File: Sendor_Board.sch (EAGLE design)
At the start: 36 parts, among them Q1 8.000Mhz, U1 PIC32MX795F512H-80I/PT, U2 SHT25, U3 MPL115A2, U4 MRF24J40MA, X1 MINI-USB-SHIELD-UX60A-MB-5ST

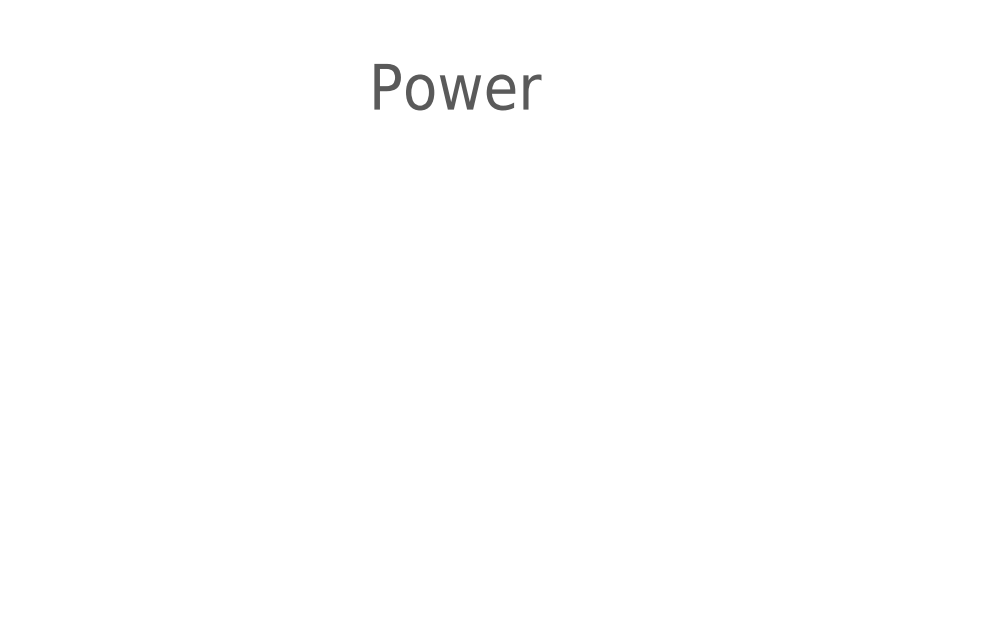
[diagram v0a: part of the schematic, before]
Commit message: Add 3,3V decoupling capacitor
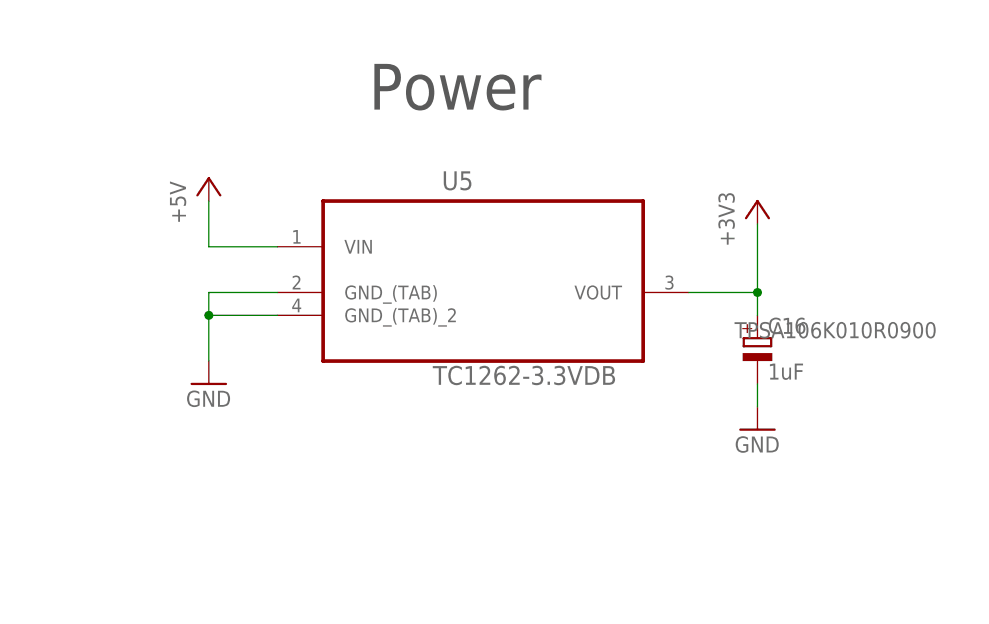
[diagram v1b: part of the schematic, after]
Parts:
- added C16: 1uF, resistor:CPOL-EUA/3216-18W
- added U5: TC1262-3.3VDB, pfo:TC1262-3.3VDB
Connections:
- net +3V3: now also C16.+, U5.VOUT
- net +5V: now also U5.VIN
- net GND: now also C16.-, U5.GND_(TAB), U5.GND_(TAB)_2
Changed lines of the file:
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@@
 <part name="X2" library="con-phoenix-254" deviceset="MPT2" device=""/>
 <part name="FRAME1" library="frames" deviceset="A3L-LOC" device=""/>
+<part name="U5" library="pfo" deviceset="TC1262-3.3VDB" device=""/>
+<part name="P+3" library="supply1" deviceset="+5V" device=""/>
+<part name="GND15" library="supply1" deviceset="GND" device=""/>
+<part name="+3V6" library="supply1" deviceset="+3V3" device=""/>
+<part name="C16" library="resistor" deviceset="CPOL-EU" device="A/3216-18W" value="1uF">
+<attribute name="TYPE" value="TPSA106K010R0900"/>
+</part>
+<part name="GND16" library="supply1" deviceset="GND" device=""/>
 </parts>
 <sheets>
@@
 <instance part="X2" gate="-2" x="144.78" y="-88.9"/>
 <instance part="FRAME1" gate="G$1" x="-111.76" y="-142.24"/>
+<instance part="U5" gate="A" x="208.28" y="-33.02"/>
+<instance part="P+3" gate="1" x="177.8" y="-25.4"/>
+<instance part="GND15" gate="1" x="177.8" y="-48.26"/>
+<instance part="+3V6" gate="G$1" x="238.76" y="-27.94"/>
+<instance part="C16" gate="G$1" x="238.76" y="-43.18">
+<attribute name="TYPE" x="236.22" y="-43.18" size="1.778" layer="96"/>
+</instance>
+<instance part="GND16" gate="1" x="238.76" y="-53.34"/>
 </instances>
 <busses>
@@
 <wire x1="68.58" y1="-124.46" x2="68.58" y2="-127" width="0.1524" layer="91"/>
 </segment>
+<segment>
+<pinref part="U5" gate="A" pin="GND_(TAB)"/>
+<pinref part="GND15" gate="1" pin="GND"/>
+<wire x1="185.42" y1="-38.1" x2="177.8" y2="-38.1" width="0.1524" layer="91"/>
+<wire x1="177.8" y1="-38.1" x2="177.8" y2="-40.64" width="0.1524" layer="91"/>
+<pinref part="U5" gate="A" pin="GND_(TAB)_2"/>
+<wire x1="177.8" y1="-40.64" x2="177.8" y2="-45.72" width="0.1524" layer="91"/>
+<wire x1="185.42" y1="-40.64" x2="177.8" y2="-40.64" width="0.1524" layer="91"/>
+<junction x="177.8" y="-40.64"/>
+</segment>
+<segment>
+<pinref part="C16" gate="G$1" pin="-"/>
+<pinref part="GND16" gate="1" pin="GND"/>
+<wire x1="238.76" y1="-48.26" x2="238.76" y2="-50.8" width="0.1524" layer="91"/>
+</segment>
 </net>
 <net name="+3V3" class="0">
@@
 <junction x="96.52" y="-15.24"/>
 </segment>
+<segment>
+<pinref part="+3V6" gate="G$1" pin="+3V3"/>
+<wire x1="238.76" y1="-30.48" x2="238.76" y2="-38.1" width="0.1524" layer="91"/>
+<pinref part="U5" gate="A" pin="VOUT"/>
+<wire x1="238.76" y1="-38.1" x2="231.14" y2="-38.1" width="0.1524" layer="91"/>
+<pinref part="C16" gate="G$1" pin="+"/>
+<wire x1="238.76" y1="-40.64" x2="238.76" y2="-38.1" width="0.1524" layer="91"/>
+<junction x="238.76" y="-38.1"/>
+</segment>
 </net>
 <net name="N$1" class="0">
@@
 <wire x1="-93.98" y1="-5.08" x2="-83.82" y2="-5.08" width="0.1524" layer="91"/>
 </segment>
-</net>
+<segment>
+<pinref part="U5" gate="A" pin="VIN"/>
+<pinref part="P+3" gate="1" pin="+5V"/>
+<wire x1="185.42" y1="-33.02" x2="177.8" y2="-33.02" width="0.1524" layer="91"/>
+<wire x1="177.8" y1="-33.02" x2="177.8" y2="-27.94" width="0.1524" layer="91"/>
+</segment>
+</net>

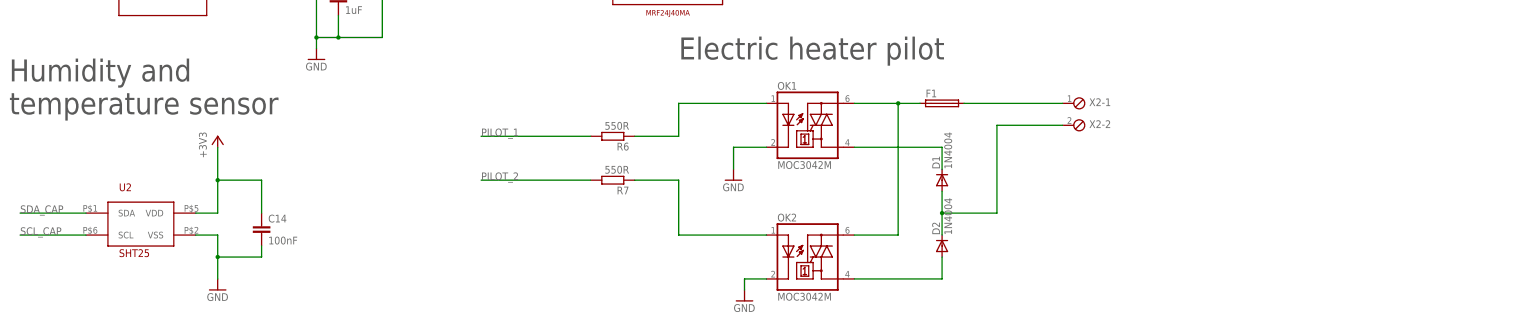
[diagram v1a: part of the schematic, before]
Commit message: Insert Power convertor
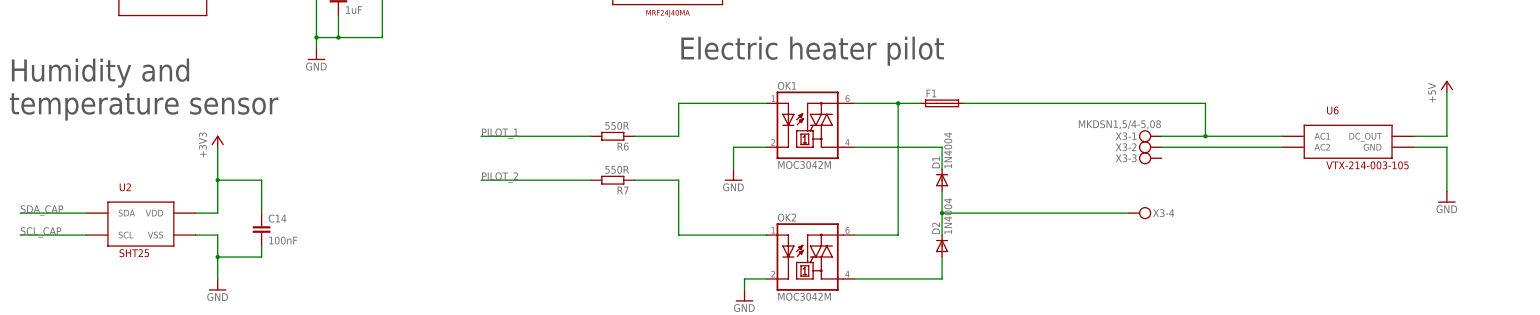
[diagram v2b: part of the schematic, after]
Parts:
- removed X2: (no value), con-phoenix-254:MPT2
- added U6: VTX-214-003-105, pfo:VTX-214-003-105
- added X3: MKDSN1,5/4-5,08, con-phoenix-508:MKDSN1,5/4-5,08
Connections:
- new net +5V_USB: X1G$1.1
- new net N$17: U6.AC2, X3-2.KL
- net +5V: now also U6.DC_OUT; no longer X1G$1.1
- net GND: now also U6.GND
- net N$11: now also U6.AC1, X3-1.KL; no longer X2-1.1
- net N$15: now also X3-4.KL; no longer X2-2.1
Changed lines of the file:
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@@
 <part name="D1" library="diode" deviceset="1N4004" device=""/>
 <part name="D2" library="diode" deviceset="1N4004" device=""/>
-<part name="X2" library="con-phoenix-254" deviceset="MPT2" device=""/>
 <part name="FRAME1" library="frames" deviceset="A3L-LOC" device=""/>
 <part name="U5" library="pfo" deviceset="TC1262-3.3VDB" device=""/>
@@
 </part>
 <part name="GND16" library="supply1" deviceset="GND" device=""/>
+<part name="X3" library="con-phoenix-508" deviceset="MKDSN1,5/4-5,08" device=""/>
+<part name="U6" library="pfo" deviceset="VTX-214-003-105" device=""/>
+<part name="GND17" library="supply1" deviceset="GND" device=""/>
+<part name="P+4" library="supply1" deviceset="+5V" device=""/>
 </parts>
 <sheets>
@@
 <instance part="D1" gate="1" x="114.3" y="-101.6" rot="R90"/>
 <instance part="D2" gate="1" x="114.3" y="-116.84" rot="R90"/>
-<instance part="X2" gate="-1" x="144.78" y="-83.82"/>
-<instance part="X2" gate="-2" x="144.78" y="-88.9"/>
 <instance part="FRAME1" gate="G$1" x="-111.76" y="-142.24"/>
 <instance part="U5" gate="A" x="208.28" y="-33.02"/>
@@
 </instance>
 <instance part="GND16" gate="1" x="238.76" y="-53.34"/>
+<instance part="X3" gate="-1" x="162.56" y="-91.44" rot="R180"/>
+<instance part="X3" gate="-2" x="162.56" y="-93.98" rot="R180"/>
+<instance part="X3" gate="-3" x="162.56" y="-96.52" rot="R180"/>
+<instance part="X3" gate="-4" x="160.02" y="-109.22"/>
+<instance part="U6" gate="G$1" x="208.28" y="-93.98"/>
+<instance part="GND17" gate="1" x="231.14" y="-106.68"/>
+<instance part="P+4" gate="1" x="231.14" y="-78.74"/>
 </instances>
 <busses>
@@
 <wire x1="238.76" y1="-48.26" x2="238.76" y2="-50.8" width="0.1524" layer="91"/>
 </segment>
+<segment>
+<pinref part="U6" gate="G$1" pin="GND"/>
+<pinref part="GND17" gate="1" pin="GND"/>
+<wire x1="223.52" y1="-93.98" x2="231.14" y2="-93.98" width="0.1524" layer="91"/>
+<wire x1="231.14" y1="-93.98" x2="231.14" y2="-104.14" width="0.1524" layer="91"/>
+</segment>
 </net>
 <net name="+3V3" class="0">
@@
 </segment>
 <segment>
-<pinref part="P+1" gate="1" pin="+5V"/>
-<pinref part="X1" gate="G$1" pin="1"/>
-<wire x1="-93.98" y1="5.08" x2="-93.98" y2="-5.08" width="0.1524" layer="91"/>
-<wire x1="-93.98" y1="-5.08" x2="-83.82" y2="-5.08" width="0.1524" layer="91"/>
-</segment>
-<segment>
 <pinref part="U5" gate="A" pin="VIN"/>
 <pinref part="P+3" gate="1" pin="+5V"/>
 <wire x1="185.42" y1="-33.02" x2="177.8" y2="-33.02" width="0.1524" layer="91"/>
 <wire x1="177.8" y1="-33.02" x2="177.8" y2="-27.94" width="0.1524" layer="91"/>
+</segment>
+<segment>
+<pinref part="P+4" gate="1" pin="+5V"/>
+<wire x1="231.14" y1="-81.28" x2="231.14" y2="-91.44" width="0.1524" layer="91"/>
+<pinref part="U6" gate="G$1" pin="DC_OUT"/>
+<wire x1="231.14" y1="-91.44" x2="223.52" y2="-91.44" width="0.1524" layer="91"/>
 </segment>
 </net>
@@
 <segment>
 <pinref part="F1" gate="1" pin="2"/>
-<wire x1="119.38" y1="-83.82" x2="142.24" y2="-83.82" width="0.1524" layer="91"/>
-<pinref part="X2" gate="-1" pin="1"/>
+<pinref part="X3" gate="-1" pin="KL"/>
+<wire x1="165.1" y1="-91.44" x2="175.26" y2="-91.44" width="0.1524" layer="91"/>
+<wire x1="175.26" y1="-91.44" x2="175.26" y2="-83.82" width="0.1524" layer="91"/>
+<wire x1="175.26" y1="-83.82" x2="119.38" y2="-83.82" width="0.1524" layer="91"/>
+<junction x="175.26" y="-91.44"/>
+<wire x1="175.26" y1="-91.44" x2="193.04" y2="-91.44" width="0.1524" layer="91"/>
+<pinref part="U6" gate="G$1" pin="AC1"/>
 </segment>
 </net>
@@
 <wire x1="114.3" y1="-114.3" x2="114.3" y2="-109.22" width="0.1524" layer="91"/>
 <wire x1="114.3" y1="-109.22" x2="114.3" y2="-104.14" width="0.1524" layer="91"/>
-<wire x1="114.3" y1="-109.22" x2="127" y2="-109.22" width="0.1524" layer="91"/>
-<wire x1="127" y1="-109.22" x2="127" y2="-88.9" width="0.1524" layer="91"/>
-<wire x1="127" y1="-88.9" x2="142.24" y2="-88.9" width="0.1524" layer="91"/>
+<wire x1="114.3" y1="-109.22" x2="157.48" y2="-109.22" width="0.1524" layer="91"/>
 <junction x="114.3" y="-109.22"/>
-<pinref part="X2" gate="-2" pin="1"/>
-</segment>
-</net>
+<pinref part="X3" gate="-4" pin="KL"/>
+</segment>
+</net>
+<net name="N$17" class="0">
+<segment>
+<pinref part="X3" gate="-2" pin="KL"/>
+<wire x1="165.1" y1="-93.98" x2="193.04" y2="-93.98" width="0.1524" layer="91"/>
+<pinref part="U6" gate="G$1" pin="AC2"/>
+</segment>
+</net>
+<net name="+5V_USB" class="0">
+<segment>
+<pinref part="P+1" gate="1" pin="+5V"/>
+<pinref part="X1" gate="G$1" pin="1"/>
+<wire x1="-93.98" y1="5.08" x2="-93.98" y2="-5.08" width="0.1524" layer="91"/>
+<wire x1="-93.98" y1="-5.08" x2="-83.82" y2="-5.08" width="0.1524" layer="91"/>
+</segment>
+</net>

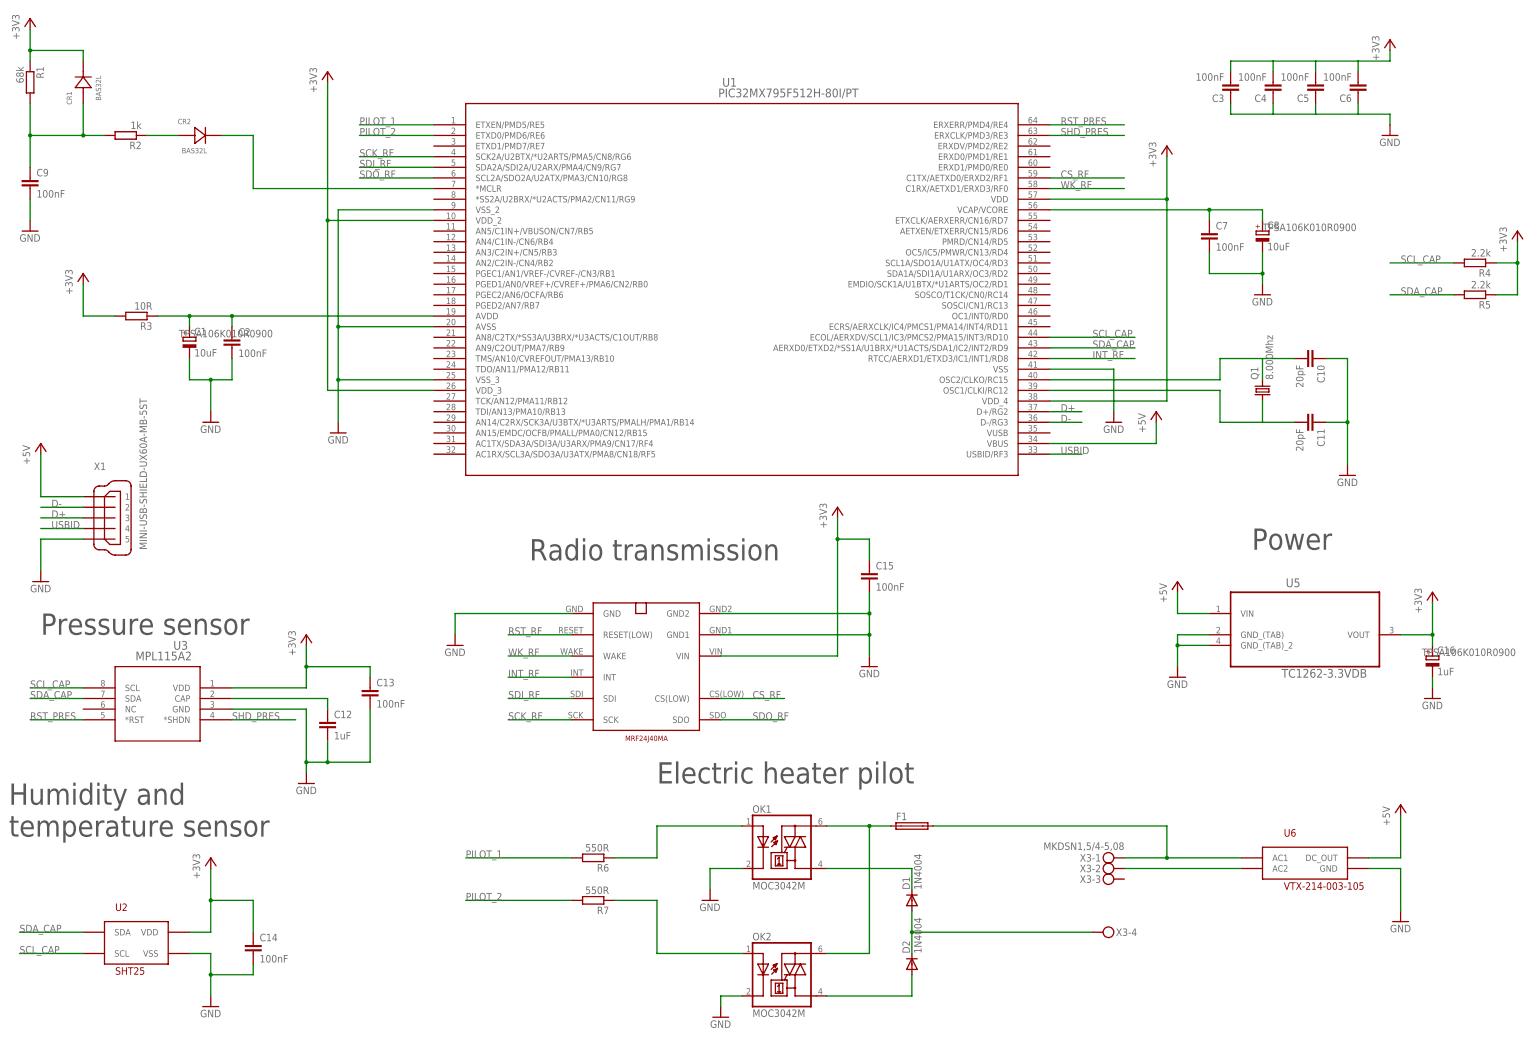
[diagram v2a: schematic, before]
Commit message: insert led
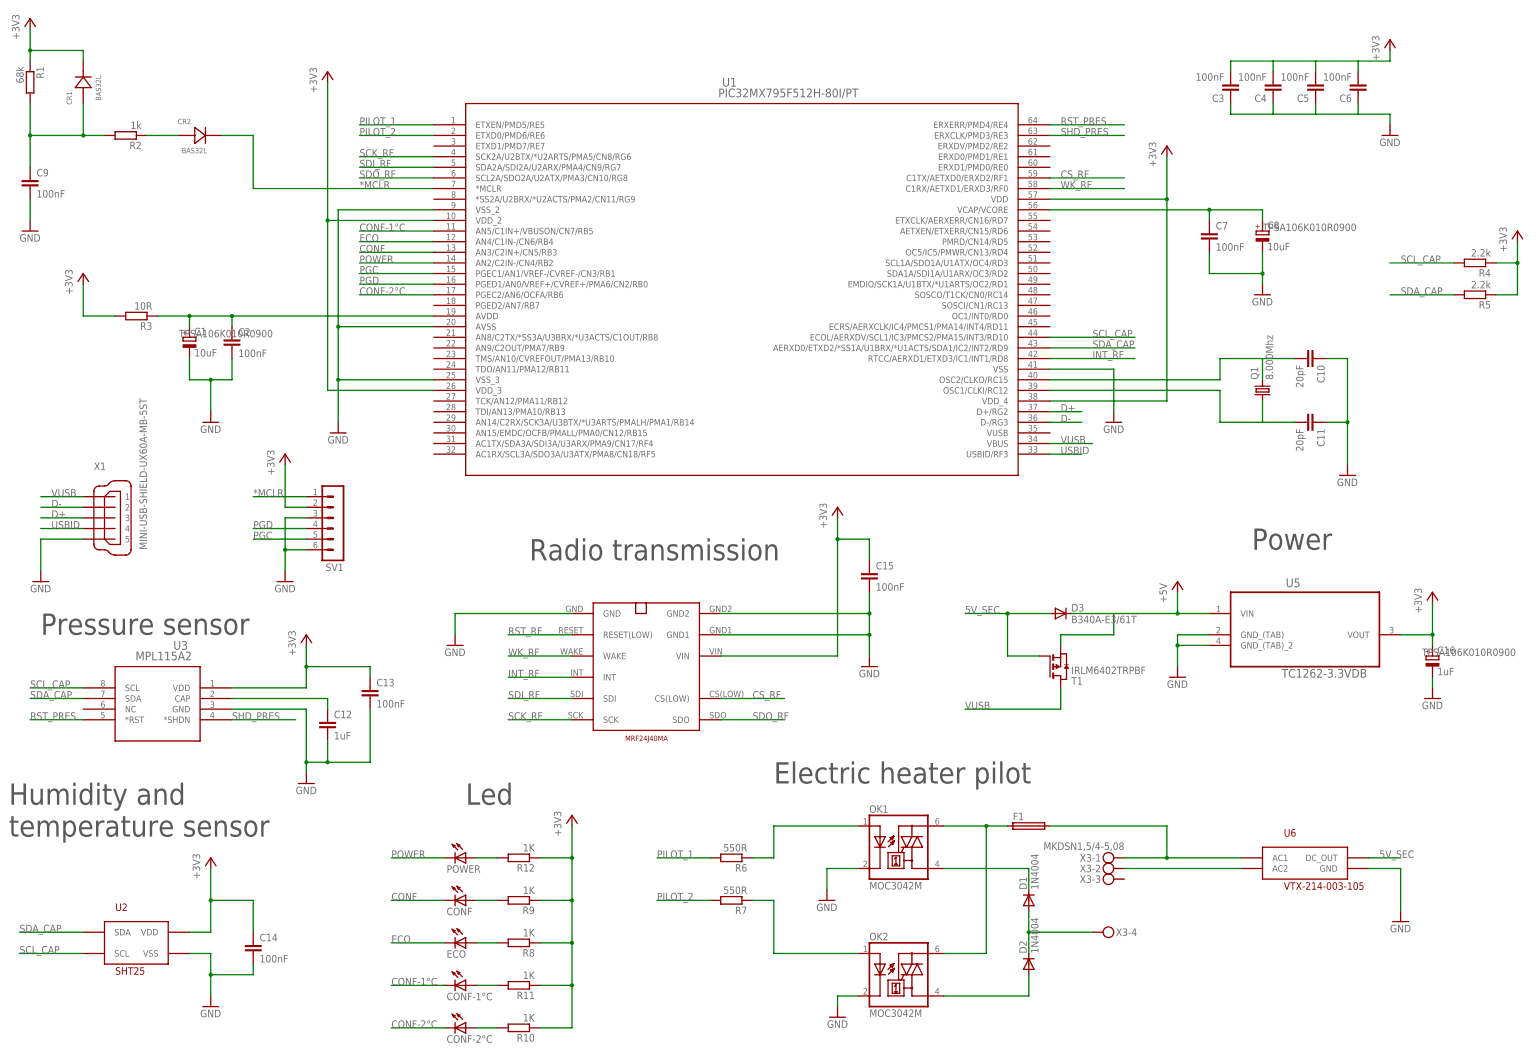
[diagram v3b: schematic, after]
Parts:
- added CONF, CONF-1°C, CONF-2°C, ECO, POWER: (no value), led:LEDCHIP-LED0805
- added D3: B340A-E3/61T, diode:DIODE-DO214AC
- added R10, R11, R12, R8, R9: 1K, resistor:R-EU_R1206
- added SV1: (no value), con-lstb:MA06-1
- added T1: IRLM6402TRPBF, zetex:PMOSSOT23
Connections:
- removed net +5V_USB: X1G$1.1
- new net *MCLR: CR2.CATHODE, SV1.1, U1.*MCLR
- new net 5V_SEC: D3.A, T1.G, U6.DC_OUT
- new net CONF: CONF.C, U1.AN3/C2IN+/CN5/RB3
- new net CONF-1°C: CONF-1°C.C, U1.AN5/C1IN+/VBUSON/CN7/RB5
- new net CONF-2°C: CONF-2°C.C, U1.PGEC2/AN6/OCFA/RB6
- new net ECO: ECO.C, U1.AN4/C1IN-/CN6/RB4
- new net N$16: CONF-1°C.A, R11.2
- new net N$18: ECO.A, R8.2
- new net N$19: CONF.A, R9.2
- new net N$20: POWER.A, R12.2
- new net PGC: SV1.5, U1.PGEC1/AN1/VREF-/CVREF-/CN3/RB1
- new net PGD: SV1.4, U1.PGED1/AN0/VREF+/CVREF+/PMA6/CN2/RB0
- new net POWER: POWER.C, U1.AN2/C2IN-/CN4/RB2
- new net VUSB: T1.D, U1.VBUS, X1G$1.1
- net +3V3: now also R10.1, R11.1, R12.1, R8.1, R9.1, SV1.2
- net +5V: now also D3.C, T1.S; no longer U1.VBUS, U6.DC_OUT
- net GND: now also SV1.3, SV1.6
- net N$6: now also CONF-2°C.A, R10.2; no longer CR2.CATHODE, U1.*MCLR
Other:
- note added: "Led"
- moved on the sheet: D1, D2, F1, OK1, OK2, R6, R7
